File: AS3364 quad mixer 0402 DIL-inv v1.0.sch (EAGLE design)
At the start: 48 parts, among them IC1 TL072JD, IC2 TL072JD

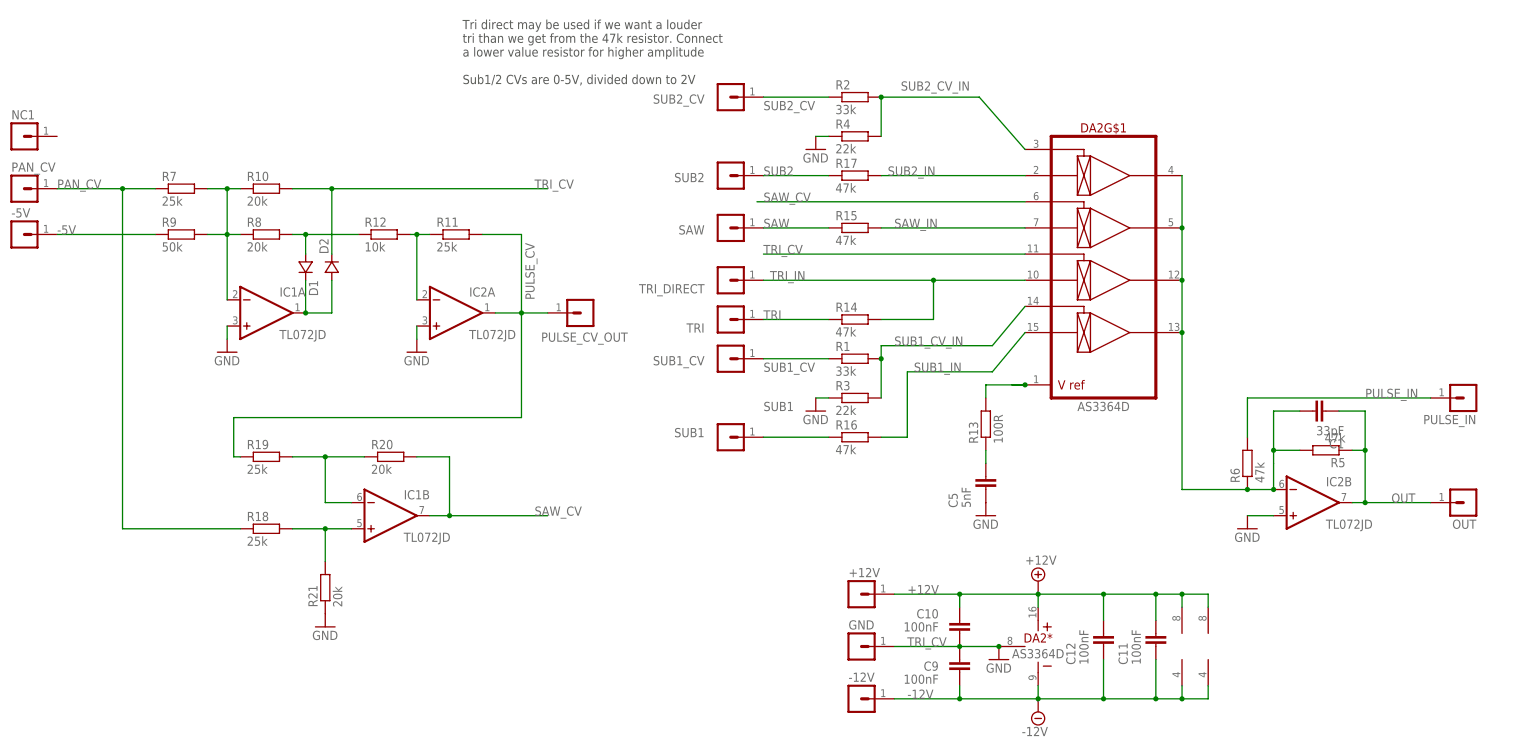
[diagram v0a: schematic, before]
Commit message: Checked most things, changed CV input resistors, added cap to mixer output
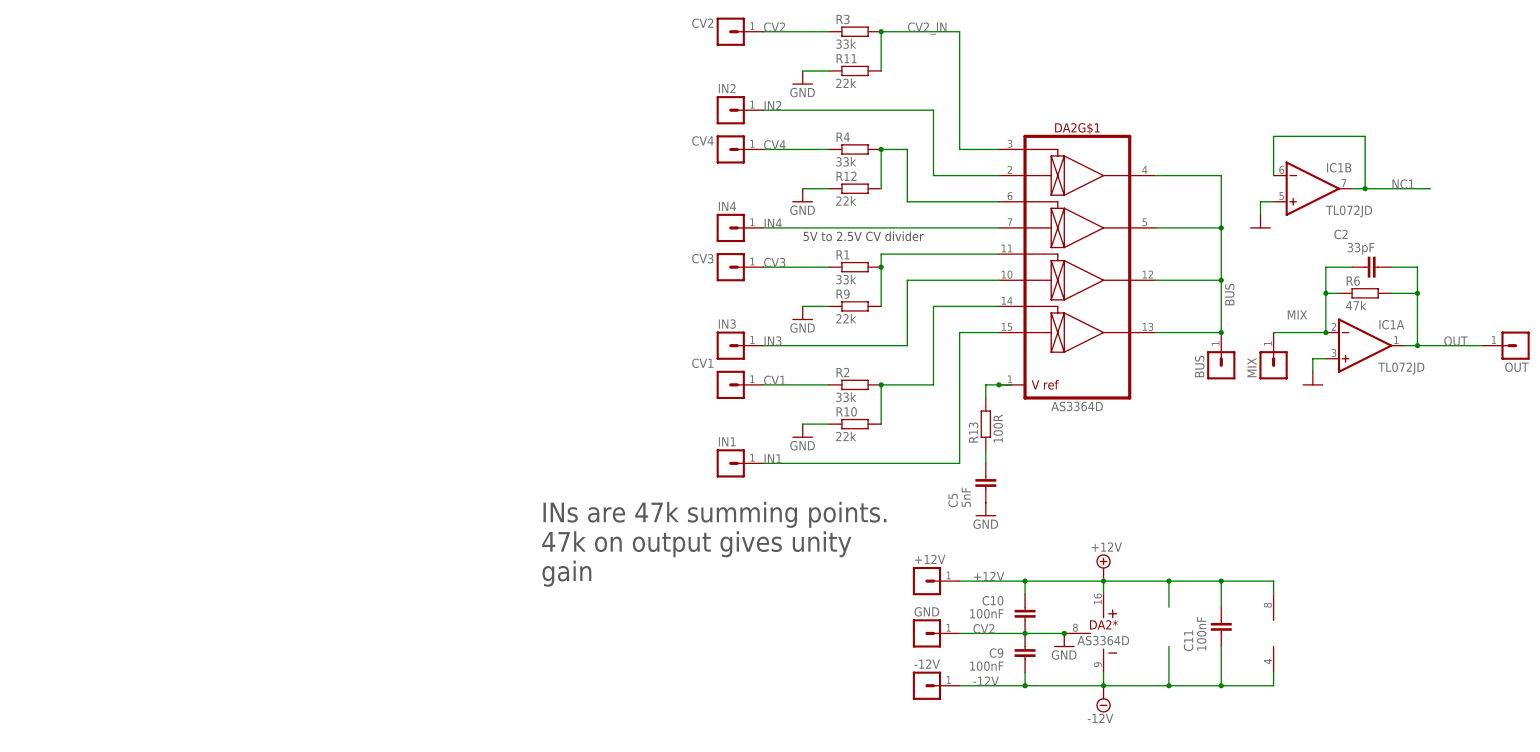
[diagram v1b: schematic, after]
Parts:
- removed -5V, NC1, PAN_CV, PULSE_CV_OUT, PULSE_IN, SUB1, SUB1_CV, SUB2, SUB2_CV, TRI, TRI_DIRECT: (no value), joakim:MA01-1JP
- removed C1: 33pF, rcl:C-EUC0402
- removed C12: 100nF, rcl:C-EUC0402
- removed D1, D2: (no value), joakim:DIODESOD323
- removed IC2: TL072JD, joakim:TL072JD
- removed R14, R15, R16, R17, R5: 47k, rcl:R-EU_R0402
- removed R18, R19, R7: 25k, rcl:R-EU_R0402
- removed R20, R21, R8: 20k, rcl:R-EU_R0402
- added BUS, CV1, CV2, CV3, CV4, IN1, IN2, IN3, MIX: (no value), joakim:MA01-1JP
- added C2: 33pF, rcl:C-EUC0402
- R10: value 20k -> 22k
- R11: value 25k -> 22k
- R12: value 10k -> 22k
- R3, R4: value 22k -> 33k
- R9: value 50k -> 22k
- renumbered SAW to IN4
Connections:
- removed net -5V: -5V.1, R9.1
- removed net MIX_BUS: C1.2, DA2G$1.OUT1, DA2G$1.OUT2, DA2G$1.OUT3, DA2G$1.OUT4, IC2B.-IN, R5.2, R6.1
- removed net N$11: IC1B.+IN, R18.2, R21.2
- removed net N$15: IC1B.-IN, R19.2, R20.1
- removed net N$18: IC2A.-IN, R11.1, R12.2
- removed net N$19: D1.A, R12.1, R8.2
- removed net N$6: D1.C, D2.A, IC1A.OUT
- removed net N$8: IC1A.-IN, R10.1, R7.2, R8.1, R9.2
- removed net PAN_CV: PAN_CV.1, R18.1, R7.1
- removed net PULSE_CV: IC2A.OUT, PULSE_CV_OUT.1, R11.2, R19.1
- removed net PULSE_IN: PULSE_IN.1, R6.2
- removed net SAW: IN4.1, R15.1
- removed net SAW_CV: DA2G$1.CV2, IC1B.OUT, R20.2
- removed net SAW_IN: DA2G$1.IN2, R15.2
- removed net SUB1: R16.1, SUB1.1
- removed net SUB1_CV: R1.1, SUB1_CV.1
- removed net SUB1_CV_IN: DA2G$1.CV4, R1.2, R3.2
- removed net SUB1_IN: DA2G$1.IN4, R16.2
- removed net SUB2: R17.1, SUB2.1
- removed net SUB2_CV: R2.1, SUB2_CV.1
- removed net SUB2_CV_IN: DA2G$1.CV1, R2.2, R4.2
- removed net SUB2_IN: DA2G$1.IN1, R17.2
- removed net TRI: R14.1, TRI.1
- removed net TRI_CV: D2.C, DA2G$1.CV3, R10.2
- removed net TRI_IN: DA2G$1.IN3, R14.2, TRI_DIRECT.1
- new net BUS: BUS.1, DA2G$1.OUT1, DA2G$1.OUT2, DA2G$1.OUT3, DA2G$1.OUT4
- new net CV1: CV1.1, R2.1
- new net CV2: CV2.1, R3.1
- new net CV2_IN: DA2G$1.CV1, R11.2, R3.2
- new net CV3: CV3.1, R1.1
- new net CV4: CV4.1, R4.1
- new net IN1: DA2G$1.IN4, IN1.1
- new net IN2: DA2G$1.IN1, IN2.1
- new net IN3: DA2G$1.IN3, IN3.1
- new net IN4: DA2G$1.IN2, IN4.1
- new net MIX: C2.1, IC1A.-IN, MIX.1, R6.1
- new net N$10: DA2G$1.CV2, R12.2, R4.2
- new net N$12: DA2G$1.CV3, R1.2, R9.2
- new net N$21: DA2G$1.CV4, R10.2, R2.2
- new net NC1: IC1B.-IN, IC1B.OUT
- net +12V: no longer C12.2, IC2P.V+
- net -12V: no longer C12.1, IC2P.V-
- net GND: now also IC1B.+IN, R10.1, R11.1, R12.1, R9.1; no longer IC2A.+IN, IC2B.+IN, R21.1, R3.1, R4.1
- net OUT: now also C2.2, IC1A.OUT, R6.2; no longer C1.1, IC2B.OUT, R5.1
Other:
- note added: "5V to 2.5V CV divider"
- note added: "INs are 47k summing points. 47k on output gives unity gain"
- note removed: "Tri direct may be used if we want a louder tri than we get from the 47k resistor. Connect a lower value resistor for higher amplitude Sub1/2 CVs are 0-5V, divided down to 2V"
- moved on the sheet: +12V, -12V, C10, C11, C9, DA2*, DA2G$1, GND, IC1A, IC1B, OUT, R1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

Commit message: Almost finished bom/cpl
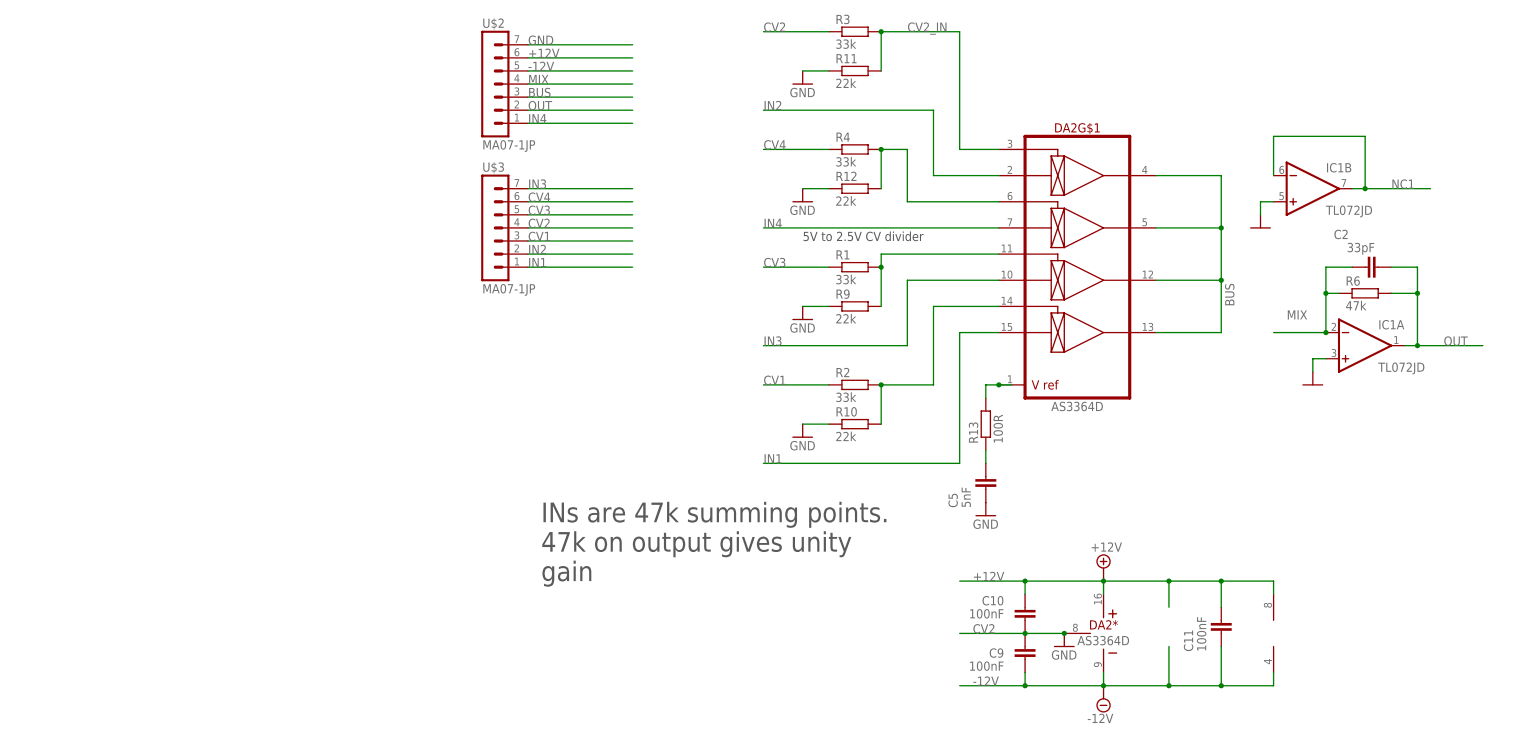
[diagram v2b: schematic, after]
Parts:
- removed +12V, -12V, BUS, CV1, CV2, CV3, CV4, GND, IN1, IN2, IN3, IN4, MIX, OUT: (no value), joakim:MA01-1JP
- added U$2, U$3: MA07-1JP, joakim:MA07-1JP
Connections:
- net +12V: now also U$2.6; no longer +12V.1
- net -12V: now also U$2.5; no longer -12V.1
- net BUS: now also U$2.3; no longer BUS.1
- net CV1: now also U$3.3; no longer CV1.1
- net CV2: now also U$3.4; no longer CV2.1
- net CV3: now also U$3.5; no longer CV3.1
- net CV4: now also U$3.6; no longer CV4.1
- net GND: now also U$2.7; no longer GND.1
- net IN1: now also U$3.1; no longer IN1.1
- net IN2: now also U$3.2; no longer IN2.1
- net IN3: now also U$3.7; no longer IN3.1
- net IN4: now also U$2.1; no longer IN4.1
- net MIX: now also U$2.4; no longer MIX.1
- net OUT: now also U$2.2; no longer OUT.1
